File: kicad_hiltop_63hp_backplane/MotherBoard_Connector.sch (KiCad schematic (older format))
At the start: 7 parts, among them J10 Conn_01x02, J7 HILTOP_PCIE-64_CONN, J8 Conn_02x04_Odd_Even, J9 Conn_02x02_Counter_Clockwise

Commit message: Rev A
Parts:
- J10: symbol Connector1:Conn_01x02 -> hiltop_backplane_brd-rescue:Conn_01x02-Connector1; Devtank (none) -> 709-002
- J7: footprint GTI_Footprint_Lib:CONN PCI EXP FEMALE 64POS 0.039 -> Devtank_PCB_Lib:CONN PCI EXP FEMALE 64POS 0.039; symbol gti_Lattice:HILTOP_PCIE-64_CONN -> hiltop_backplane_brd-rescue:HILTOP_PCIE-64_CONN-gti_Lattice
- J8: symbol Connector1:Conn_02x04_Odd_Even -> hiltop_backplane_brd-rescue:Conn_02x04_Odd_Even-Connector1; Devtank (none) -> 709-005
- J9: symbol Connector1:Conn_02x02_Counter_Clockwise -> hiltop_backplane_brd-rescue:Conn_02x02_Counter_Clockwise-Connector1; Devtank (none) -> 709-006
- R45: symbol device:Polyfuse -> hiltop_backplane_brd-rescue:Polyfuse-device; Devtank (none) -> 101-005
- R46, R47: symbol device:Polyfuse -> hiltop_backplane_brd-rescue:Polyfuse-device; Devtank (none) -> 101-007
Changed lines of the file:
@@
 -5V
 $Comp
-L gti_Lattice:HILTOP_PCIE-64_CONN J7
+L hiltop_backplane_brd-rescue:HILTOP_PCIE-64_CONN-gti_Lattice J7
 U 1 1 5C13457D
 P 3575 2725
 F 0 "J7" H 3575 4640 50  0000 C CNN
 F 1 "HILTOP_PCIE-64_CONN" H 3575 4549 50  0000 C CNN
-F 2 "GTI_Footprint_Lib:CONN PCI EXP FEMALE 64POS 0.039" H 2925 4575 50  0001 C CNN
+F 2 "Devtank_PCB_Lib:CONN PCI EXP FEMALE 64POS 0.039" H 2925 4575 50  0001 C CNN
 F 3 "" H 3075 4675 50  0001 C CNN
 	1    3575 2725
@@
 Connection ~ 4650 2175
 $Comp
-L Connector1:Conn_02x04_Odd_Even J8
+L hiltop_backplane_brd-rescue:Conn_02x04_Odd_Even-Connector1 J8
 U 1 1 5C155D60
 P 8400 1825
@@
 F 2 "Connector_Molex:Molex_Mini-Fit_Jr_5566-08A_2x04_P4.20mm_Vertical" H 8400 1825 50  0001 C CNN
 F 3 "~" H 8400 1825 50  0001 C CNN
+F 4 "709-005" H 0   0   50  0001 C CNN "Devtank"
 	1    8400 1825
 	1    0    0    -1
 $EndComp
 $Comp
-L Connector1:Conn_02x02_Counter_Clockwise J9
+L hiltop_backplane_brd-rescue:Conn_02x02_Counter_Clockwise-Connector1 J9
 U 1 1 5C155E73
 P 8425 2700
@@
 F 2 "Connector_Molex:Molex_Mini-Fit_Jr_5566-04A_2x02_P4.20mm_Vertical" H 8425 2700 50  0001 C CNN
 F 3 "~" H 8425 2700 50  0001 C CNN
+F 4 "709-006" H 0   0   50  0001 C CNN "Devtank"
 	1    8425 2700
 	1    0    0    -1
 $EndComp
 $Comp
-L Connector1:Conn_01x02 J10
+L hiltop_backplane_brd-rescue:Conn_01x02-Connector1 J10
 U 1 1 5C155F47
 P 8475 3425
@@
 F 2 "Connector_Molex:Molex_Mini-Fit_Jr_5566-02A2_2x01_P4.20mm_Vertical" H 8475 3425 50  0001 C CNN
 F 3 "~" H 8475 3425 50  0001 C CNN
+F 4 "709-002" H 0   0   50  0001 C CNN "Devtank"
 	1    8475 3425
 	1    0    0    -1
@@
 	8700 2025 8925 2025
 $Comp
-L device:Polyfuse R47
+L hiltop_backplane_brd-rescue:Polyfuse-device R47
 U 1 1 5C36D98A
 P 9100 2700
@@
 F 2 "Resistor_SMD:R_1206_3216Metric" H 9150 2500 50  0001 L CNN
 F 3 "" H 9100 2700 50  0001 C CNN
+F 4 "101-007" H 0   0   50  0001 C CNN "Devtank"
 	1    9100 2700
 	0    1    1    0
 $EndComp
 $Comp
-L device:Polyfuse R45
+L hiltop_backplane_brd-rescue:Polyfuse-device R45
 U 1 1 5C36DB02
 P 7950 2700
@@
 F 2 "Resistor_SMD:R_0603_1608Metric" H 8000 2500 50  0001 L CNN
 F 3 "" H 7950 2700 50  0001 C CNN
+F 4 "101-005" H 0   0   50  0001 C CNN "Devtank"
 	1    7950 2700
 	0    1    1    0
 $EndComp
 $Comp
-L device:Polyfuse R46
+L hiltop_backplane_brd-rescue:Polyfuse-device R46
 U 1 1 5C36DBE2
 P 7950 2800
@@
 F 2 "Resistor_SMD:R_1206_3216Metric" H 8000 2600 50  0001 L CNN
 F 3 "" H 7950 2800 50  0001 C CNN
+F 4 "101-007" H 0   0   50  0001 C CNN "Devtank"
 	1    7950 2800
 	0    1    1    0

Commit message: add latest changes
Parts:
- J10: symbol hiltop_backplane_brd-rescue:Conn_01x02-Connector1 -> hiltop_backplane_brd-rescue:Conn_01x02-Connector1-hiltop_backplane_brd-rescue
- J7: symbol hiltop_backplane_brd-rescue:HILTOP_PCIE-64_CONN-gti_Lattice -> hiltop_backplane_brd-rescue:HILTOP_PCIE-64_CONN-gti_Lattice-hiltop_backplane_brd-rescue
- J8: symbol hiltop_backplane_brd-rescue:Conn_02x04_Odd_Even-Connector1 -> Connector:Conn_02x04_Top_Bottom
- J9: symbol hiltop_backplane_brd-rescue:Conn_02x02_Counter_Clockwise-Connector1 -> Connector:Conn_02x02_Top_Bottom
- R45, R46, R47: symbol hiltop_backplane_brd-rescue:Polyfuse-device -> hiltop_backplane_brd-rescue:Polyfuse-device-hiltop_backplane_brd-rescue
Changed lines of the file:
@@
 EESchema Schematic File Version 4
 LIBS:hiltop_backplane_brd-cache
-EELAYER 26 0
+EELAYER 29 0
 EELAYER END
 $Descr A4 11693 8268
 encoding utf-8
 Sheet 4 6
-Title ""
-Date ""
-Rev ""
-Comp ""
+Title "63HP HILTOP Backplane"
+Date "2020-02-29"
+Rev "B"
+Comp "Devtank Ltd"
 Comment1 ""
 Comment2 ""
@@
 -5V
 $Comp
-L hiltop_backplane_brd-rescue:HILTOP_PCIE-64_CONN-gti_Lattice J7
+L hiltop_backplane_brd-rescue:HILTOP_PCIE-64_CONN-gti_Lattice-hiltop_backplane_brd-rescue J7
 U 1 1 5C13457D
 P 3575 2725
@@
 Connection ~ 4650 2175
 $Comp
-L hiltop_backplane_brd-rescue:Conn_02x04_Odd_Even-Connector1 J8
+L Connector:Conn_02x04_Top_Bottom J8
 U 1 1 5C155D60
 P 8400 1825
@@
 $EndComp
 $Comp
-L hiltop_backplane_brd-rescue:Conn_02x02_Counter_Clockwise-Connector1 J9
+L Connector:Conn_02x02_Top_Bottom J9
 U 1 1 5C155E73
 P 8425 2700
@@
 $EndComp
 $Comp
-L hiltop_backplane_brd-rescue:Conn_01x02-Connector1 J10
+L hiltop_backplane_brd-rescue:Conn_01x02-Connector1-hiltop_backplane_brd-rescue J10
 U 1 1 5C155F47
 P 8475 3425
@@
 	8700 2025 8925 2025
 $Comp
-L hiltop_backplane_brd-rescue:Polyfuse-device R47
+L hiltop_backplane_brd-rescue:Polyfuse-device-hiltop_backplane_brd-rescue R47
 U 1 1 5C36D98A
 P 9100 2700
@@
 $EndComp
 $Comp
-L hiltop_backplane_brd-rescue:Polyfuse-device R45
+L hiltop_backplane_brd-rescue:Polyfuse-device-hiltop_backplane_brd-rescue R45
 U 1 1 5C36DB02
 P 7950 2700
@@
 $EndComp
 $Comp
-L hiltop_backplane_brd-rescue:Polyfuse-device R46
+L hiltop_backplane_brd-rescue:Polyfuse-device-hiltop_backplane_brd-rescue R46
 U 1 1 5C36DBE2
 P 7950 2800

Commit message: started simplifications to design
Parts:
- J8: symbol Connector:Conn_02x04_Top_Bottom -> hiltop_backplane_brd-rescue:Conn_02x04_Top_Bottom-Connector
- J9: symbol Connector:Conn_02x02_Top_Bottom -> hiltop_backplane_brd-rescue:Conn_02x02_Top_Bottom-Connector
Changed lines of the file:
@@
 EESchema Schematic File Version 4
-LIBS:hiltop_backplane_brd-cache
-EELAYER 29 0
+EELAYER 30 0
 EELAYER END
 $Descr A4 11693 8268
@@
 Connection ~ 4650 2175
 $Comp
-L Connector:Conn_02x04_Top_Bottom J8
+L hiltop_backplane_brd-rescue:Conn_02x04_Top_Bottom-Connector J8
 U 1 1 5C155D60
 P 8400 1825
@@
 $EndComp
 $Comp
-L Connector:Conn_02x02_Top_Bottom J9
+L hiltop_backplane_brd-rescue:Conn_02x02_Top_Bottom-Connector J9
 U 1 1 5C155E73
 P 8425 2700

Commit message: updated FPGA/SOC module pinouts
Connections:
- net MBRD_GPIO12: no longer names the net of J7.B30 (GPIO12)
- net MBRD_GPIO13: no longer names the net of J7.B31 (GPIO13)
- net MBRD_GPIO14: no longer names the net of J7.A29 (GPIO14)
- net MBRD_GPIO15: no longer names the net of J7.A30 (GPIO15)
- net MBRD_GPIO16: no longer names the net of J7.A31 (GPIO16)
- net MBRD_RESERVED_0: no longer names the net of J7.A12 (RESERVED)
- net MBRD_RESERVED_1: no longer names the net of J7.A13 (RESERVED)
- net MBRD_RESERVED_2+: no longer names the net of J7.A14 (RESERVED)
- net MBRD_RESERVED_2-: no longer names the net of J7.A15 (RESERVED)
- no-connect marks 0 -> 9
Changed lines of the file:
@@
 Sheet 4 6
 Title "63HP HILTOP Backplane"
-Date "2020-02-29"
-Rev "B"
+Date "2021-02-04"
+Rev "C"
 Comp "Devtank Ltd"
 Comment1 ""
@@
 Text HLabel 2350 4175 0    60   Input ~ 0
 MBRD_SPI1_CS2
-Text HLabel 2350 4275 0    60   Input ~ 0
-MBRD_GPIO12
-Text HLabel 2350 4375 0    60   Input ~ 0
-MBRD_GPIO13
-Text HLabel 4850 4275 2    60   Input ~ 0
-MBRD_GPIO15
-Text HLabel 4850 4375 2    60   Input ~ 0
-MBRD_GPIO16
 Wire Wire Line
 	4650 1175 4650 1475
@@
 Text HLabel 4850 3375 2    60   Input ~ 0
 MBRD_SPI0_CS1
-Text HLabel 4850 2475 2    60   Input ~ 0
-MBRD_RESERVED_0
-Text HLabel 4850 2575 2    60   Input ~ 0
-MBRD_RESERVED_1
-Text HLabel 4850 2675 2    60   Input ~ 0
-MBRD_RESERVED_2+
-Text HLabel 4850 2775 2    60   Input ~ 0
-MBRD_RESERVED_2-
 Text HLabel 4850 1575 2    60   Input ~ 0
 MBRD_PSEL_0
@@
 Wire Wire Line
 	2625 3075 2350 3075
-Text HLabel 4850 4175 2    59   Input ~ 0
-MBRD_GPIO14
+NoConn ~ 4850 4175
+NoConn ~ 4850 4275
+NoConn ~ 4850 4375
+NoConn ~ 2350 4275
+NoConn ~ 2350 4375
+NoConn ~ 4850 2475
+NoConn ~ 4850 2575
+NoConn ~ 4850 2675
+NoConn ~ 4850 2775
 $EndSCHEMATC

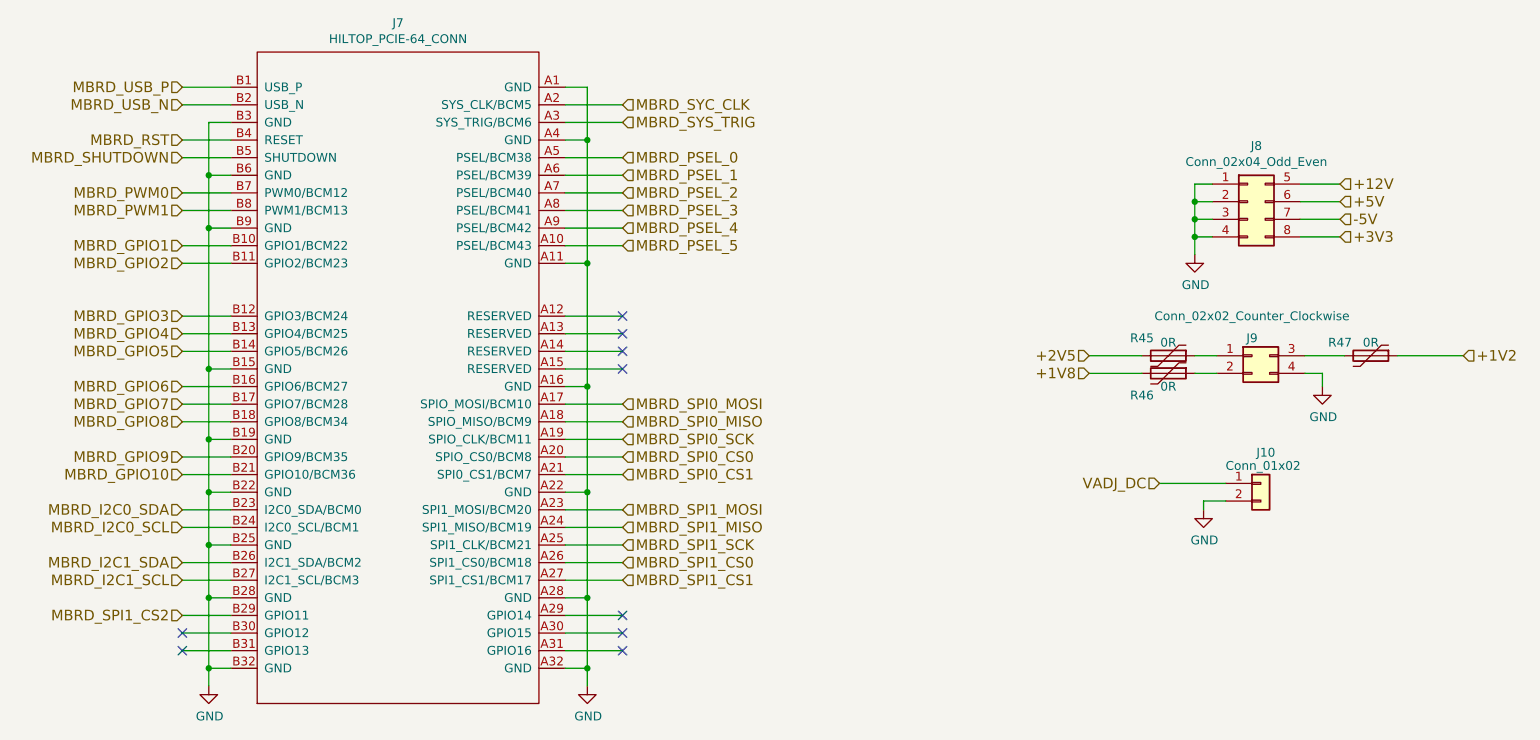
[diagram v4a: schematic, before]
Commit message: updated schematics to RevC including general tidy up
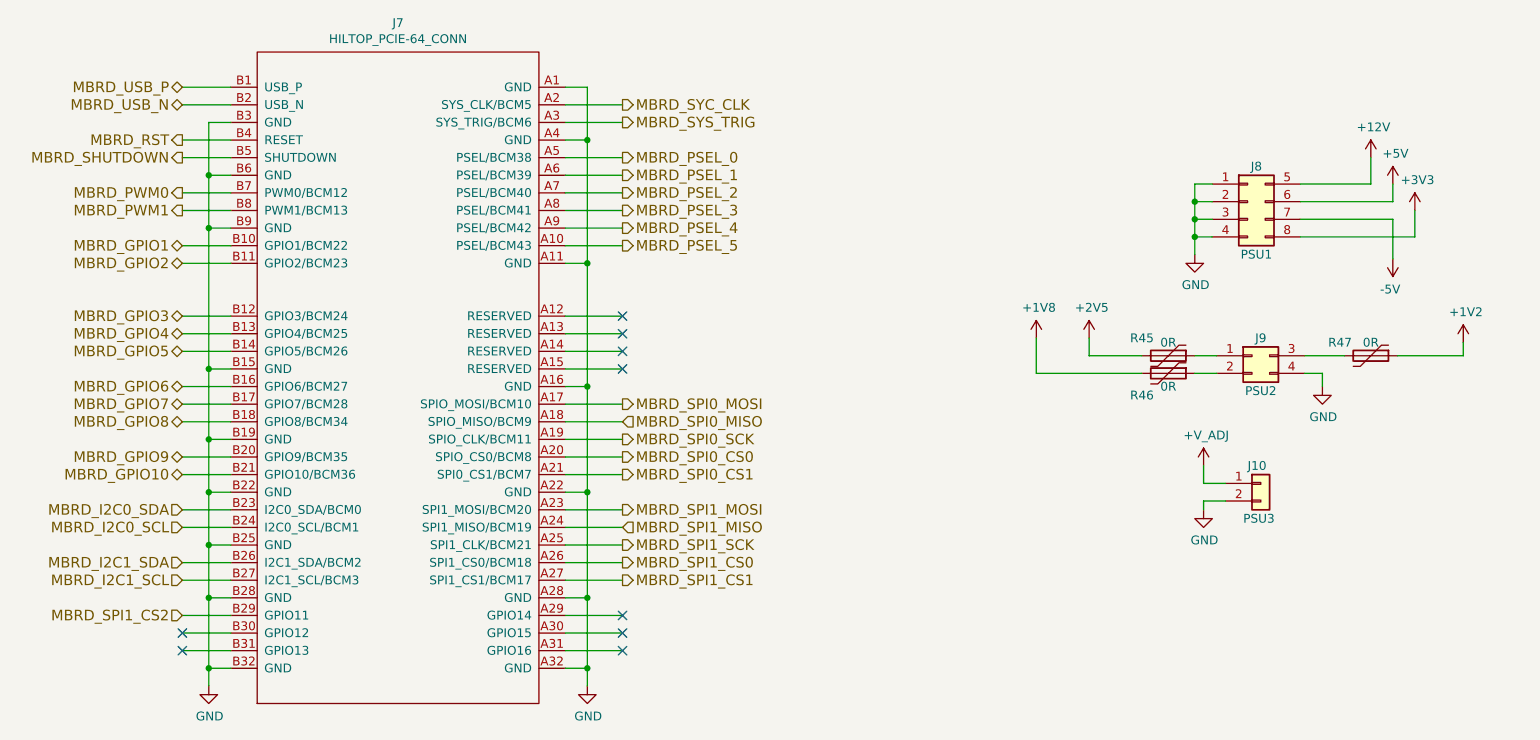
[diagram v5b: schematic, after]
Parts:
- J10: value Conn_01x02 -> PSU3
- J8: value Conn_02x04_Odd_Even -> PSU1
- J9: value Conn_02x02_Counter_Clockwise -> PSU2
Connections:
- net VADJ_DC renamed +V_ADJ
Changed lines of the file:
@@
 $Descr A4 11693 8268
 encoding utf-8
-Sheet 4 6
+Sheet 5 6
 Title "63HP HILTOP Backplane"
 Date "2021-02-04"
@@
 Wire Wire Line
 	4525 4475 4650 4475
-Text HLabel 2350 1175 0    60   Input ~ 0
+Text HLabel 2350 1175 0    60   BiDi ~ 0
 MBRD_USB_P
-Text HLabel 2350 1275 0    60   Input ~ 0
+Text HLabel 2350 1275 0    60   BiDi ~ 0
 MBRD_USB_N
 Wire Wire Line
@@
 Text HLabel 2350 3975 0    60   Input ~ 0
 MBRD_I2C1_SCL
-Text HLabel 2350 1475 0    60   Input ~ 0
+Text HLabel 2350 1475 0    60   Output ~ 0
 MBRD_RST
-Text HLabel 2350 1575 0    60   Input ~ 0
+Text HLabel 2350 1575 0    60   Output ~ 0
 MBRD_SHUTDOWN
-Text HLabel 2350 1775 0    60   Input ~ 0
+Text HLabel 2350 1775 0    60   Output ~ 0
 MBRD_PWM0
-Text HLabel 2350 1875 0    60   Input ~ 0
+Text HLabel 2350 1875 0    60   Output ~ 0
 MBRD_PWM1
-Text HLabel 2350 2075 0    60   Input ~ 0
+Text HLabel 2350 2075 0    60   BiDi ~ 0
 MBRD_GPIO1
-Text HLabel 2350 2175 0    60   Input ~ 0
+Text HLabel 2350 2175 0    60   BiDi ~ 0
 MBRD_GPIO2
-Text HLabel 2350 2475 0    60   Input ~ 0
+Text HLabel 2350 2475 0    60   BiDi ~ 0
 MBRD_GPIO3
-Text HLabel 2350 2575 0    60   Input ~ 0
+Text HLabel 2350 2575 0    60   BiDi ~ 0
 MBRD_GPIO4
-Text HLabel 2350 2675 0    60   Input ~ 0
+Text HLabel 2350 2675 0    60   BiDi ~ 0
 MBRD_GPIO5
-Text HLabel 2350 2875 0    60   Input ~ 0
+Text HLabel 2350 2875 0    60   BiDi ~ 0
 MBRD_GPIO6
-Text HLabel 2350 2975 0    60   Input ~ 0
+Text HLabel 2350 2975 0    60   BiDi ~ 0
 MBRD_GPIO7
-Text HLabel 2350 3075 0    60   Input ~ 0
+Text HLabel 2350 3075 0    60   BiDi ~ 0
 MBRD_GPIO8
-Text HLabel 2350 3275 0    60   Input ~ 0
+Text HLabel 2350 3275 0    60   BiDi ~ 0
 MBRD_GPIO9
-Text HLabel 2350 3375 0    60   Input ~ 0
+Text HLabel 2350 3375 0    60   BiDi ~ 0
 MBRD_GPIO10
-Text HLabel 4850 3575 2    60   Input ~ 0
+Text HLabel 4850 3575 2    60   Output ~ 0
 MBRD_SPI1_MOSI
 Text HLabel 4850 3675 2    60   Input ~ 0
 MBRD_SPI1_MISO
-Text HLabel 4850 3775 2    60   Input ~ 0
+Text HLabel 4850 3775 2    60   Output ~ 0
 MBRD_SPI1_SCK
-Text HLabel 4850 3875 2    60   Input ~ 0
+Text HLabel 4850 3875 2    60   Output ~ 0
 MBRD_SPI1_CS0
-Text HLabel 4850 3975 2    60   Input ~ 0
+Text HLabel 4850 3975 2    60   Output ~ 0
 MBRD_SPI1_CS1
-Text HLabel 4850 2975 2    60   Input ~ 0
+Text HLabel 4850 2975 2    60   Output ~ 0
 MBRD_SPI0_MOSI
 Text HLabel 4850 3075 2    60   Input ~ 0
 MBRD_SPI0_MISO
-Text HLabel 4850 3175 2    60   Input ~ 0
+Text HLabel 4850 3175 2    60   Output ~ 0
 MBRD_SPI0_SCK
-Text HLabel 4850 3275 2    60   Input ~ 0
+Text HLabel 4850 3275 2    60   Output ~ 0
 MBRD_SPI0_CS0
-Text HLabel 4850 3375 2    60   Input ~ 0
+Text HLabel 4850 3375 2    60   Output ~ 0
 MBRD_SPI0_CS1
-Text HLabel 4850 1575 2    60   Input ~ 0
+Text HLabel 4850 1575 2    60   Output ~ 0
 MBRD_PSEL_0
-Text HLabel 4850 1675 2    60   Input ~ 0
+Text HLabel 4850 1675 2    60   Output ~ 0
 MBRD_PSEL_1
-Text HLabel 4850 1775 2    60   Input ~ 0
+Text HLabel 4850 1775 2    60   Output ~ 0
 MBRD_PSEL_2
-Text HLabel 4850 1875 2    60   Input ~ 0
+Text HLabel 4850 1875 2    60   Output ~ 0
 MBRD_PSEL_3
-Text HLabel 4850 1975 2    60   Input ~ 0
+Text HLabel 4850 1975 2    60   Output ~ 0
 MBRD_PSEL_4
-Text HLabel 4850 2075 2    60   Input ~ 0
+Text HLabel 4850 2075 2    60   Output ~ 0
 MBRD_PSEL_5
-Text HLabel 4850 1275 2    60   Input ~ 0
+Text HLabel 4850 1275 2    60   Output ~ 0
 MBRD_SYC_CLK
-Text HLabel 4850 1375 2    60   Input ~ 0
+Text HLabel 4850 1375 2    60   Output ~ 0
 MBRD_SYS_TRIG
-Text HLabel 8925 1725 2    60   Input ~ 0
-+12V
-Text HLabel 8925 1825 2    60   Input ~ 0
-+5V
-Text HLabel 8925 2025 2    60   Input ~ 0
-+3V3
-Text HLabel 8925 1925 2    60   Input ~ 0
--5V
 $Comp
 L hiltop_backplane_brd-rescue:HILTOP_PCIE-64_CONN-gti_Lattice-hiltop_backplane_brd-rescue J7
@@
 U 1 1 5C155D60
 P 8400 1825
-F 0 "J8" H 8450 2142 50  0000 C CNN
-F 1 "Conn_02x04_Odd_Even" H 8450 2051 50  0000 C CNN
+F 0 "J8" H 8450 2025 50  0000 C CNN
+F 1 "PSU1" H 8450 1525 50  0000 C CNN
 F 2 "Connector_Molex:Molex_Mini-Fit_Jr_5566-08A_2x04_P4.20mm_Vertical" H 8400 1825 50  0001 C CNN
 F 3 "~" H 8400 1825 50  0001 C CNN
@@
 U 1 1 5C155E73
 P 8425 2700
-F 0 "J9" H 8425 2800 50  0000 C CNN
-F 1 "Conn_02x02_Counter_Clockwise" H 8425 2925 50  0000 C CNN
+F 0 "J9" H 8475 2800 50  0000 C CNN
+F 1 "PSU2" H 8475 2500 50  0000 C CNN
 F 2 "Connector_Molex:Molex_Mini-Fit_Jr_5566-04A_2x02_P4.20mm_Vertical" H 8425 2700 50  0001 C CNN
 F 3 "~" H 8425 2700 50  0001 C CNN
@@
 U 1 1 5C155F47
 P 8475 3425
-F 0 "J10" H 8450 3600 50  0000 L CNN
-F 1 "Conn_01x02" H 8275 3525 50  0000 L CNN
+F 0 "J10" H 8400 3525 50  0000 L CNN
+F 1 "PSU3" H 8375 3225 50  0000 L CNN
 F 2 "Connector_Molex:Molex_Mini-Fit_Jr_5566-02A2_2x01_P4.20mm_Vertical" H 8475 3425 50  0001 C CNN
 F 3 "~" H 8475 3425 50  0001 C CNN
@@
 Wire Wire Line
 	8825 2800 8825 2875
-Text HLabel 7500 2700 0    60   Input ~ 0
-+2V5
-Text HLabel 7500 2800 0    60   Input ~ 0
-+1V8
-Text HLabel 9625 2700 2    60   Input ~ 0
-+1V2
 $Comp
 L power:GND #PWR034
@@
 	1    0    0    -1
 $EndComp
-Text HLabel 7900 3425 0    60   Input ~ 0
-VADJ_DC
 $Comp
 L power:GND #PWR033
@@
 	8725 2700 8950 2700
 Wire Wire Line
-	7900 3425 8275 3425
-Wire Wire Line
-	8700 1725 8925 1725
-Wire Wire Line
-	8700 1825 8925 1825
-Wire Wire Line
-	8700 1925 8925 1925
-Wire Wire Line
-	8700 2025 8925 2025
+	8150 3425 8275 3425
 $Comp
 L hiltop_backplane_brd-rescue:Polyfuse-device-hiltop_backplane_brd-rescue R47
@@
 	7500 2700 7800 2700
 Wire Wire Line
-	7500 2800 7800 2800
-Wire Wire Line
 	2500 1975 2500 2775
 Wire Wire Line
@@
 NoConn ~ 4850 2675
 NoConn ~ 4850 2775
+$Comp
+L power:+2V5 #PWR?
+U 1 1 60E655E6
+P 7500 2600
+AR Path="/5A077BA2/60E655E6" Ref="#PWR?"  Part="1"
+AR Path="/5C074E5E/60E655E6" Ref="#PWR0130"  Part="1"
+F 0 "#PWR0130" H 7500 2450 50  0001 C CNN
+F 1 "+2V5" H 7515 2773 50  0000 C CNN
+F 2 "" H 7500 2600 50  0001 C CNN
+F 3 "" H 7500 2600 50  0001 C CNN
+	1    7500 2600
+	1    0    0    -1
+$EndComp
+$Comp
+L power:+3V3 #PWR?
+U 1 1 60E655EC
+P 9350 1875
+AR Path="/5A077BA2/60E655EC" Ref="#PWR?"  Part="1"
+AR Path="/5C074E5E/60E655EC" Ref="#PWR0131"  Part="1"
+F 0 "#PWR0131" H 9350 1725 50  0001 C CNN
+F 1 "+3V3" H 9365 2048 50  0000 C CNN
+F 2 "" H 9350 1875 50  0001 C CNN
+F 3 "" H 9350 1875 50  0001 C CNN
+	1    9350 1875
+	1    0    0    -1
+$EndComp
+$Comp
+L power:+1V2 #PWR?
+U 1 1 60E655F2
+P 9625 2625
+AR Path="/5A077BA2/60E655F2" Ref="#PWR?"  Part="1"
+AR Path="/5C074E5E/60E655F2" Ref="#PWR0132"  Part="1"
+F 0 "#PWR0132" H 9625 2475 50  0001 C CNN
+F 1 "+1V2" H 9640 2798 50  0000 C CNN
+F 2 "" H 9625 2625 50  0001 C CNN
+F 3 "" H 9625 2625 50  0001 C CNN
+	1    9625 2625
+	1    0    0    -1
+$EndComp
+$Comp
+L power:+1V8 #PWR?
+U 1 1 60E655F8
+P 7200 2600
+AR Path="/5A077BA2/60E655F8" Ref="#PWR?"  Part="1"
+AR Path="/5C074E5E/60E655F8" Ref="#PWR0133"  Part="1"
+F 0 "#PWR0133" H 7200 2450 50  0001 C CNN
+F 1 "+1V8" H 7215 2773 50  0000 C CNN
+F 2 "" H 7200 2600 50  0001 C CNN
+F 3 "" H 7200 2600 50  0001 C CNN
+	1    7200 2600
+	1    0    0    -1
+$EndComp
+Wire Wire Line
+	9625 2625 9625 2700
+Wire Wire Line
+	7500 2600 7500 2700
+Wire Wire Line
+	7200 2600 7200 2800
+Wire Wire Line
+	7200 2800 7800 2800
+$Comp
+L power:+5V #PWR0134
+U 1 1 62F4211C
+P 9225 1725
+F 0 "#PWR0134" H 9225 1575 50  0001 C CNN
+F 1 "+5V" H 9240 1898 50  0000 C CNN
+F 2 "" H 9225 1725 50  0001 C CNN
+F 3 "" H 9225 1725 50  0001 C CNN
+	1    9225 1725
+	1    0    0    -1
+$EndComp
+$Comp
+L Devtank:-5V #PWR0135
+U 1 1 62F42915
+P 9225 2150
+F 0 "#PWR0135" H 9225 2000 50  0001 C CNN
+F 1 "-5V" H 9240 2323 50  0000 C CNN
+F 2 "" H 9225 2150 50  0000 C CNN
+F 3 "" H 9225 2150 50  0000 C CNN
+	1    9225 2150
+	-1   0    0    1
+$EndComp
+$Comp
+L power:+12V #PWR0136
+U 1 1 62F432BB
+P 9100 1575
+F 0 "#PWR0136" H 9100 1425 50  0001 C CNN
+F 1 "+12V" H 9115 1748 50  0000 C CNN
+F 2 "" H 9100 1575 50  0001 C CNN
+F 3 "" H 9100 1575 50  0001 C CNN
+	1    9100 1575
+	1    0    0    -1
+$EndComp
+Wire Wire Line
+	9100 1725 9100 1575
+Wire Wire Line
+	8700 1725 9100 1725
+Wire Wire Line
+	9225 1825 9225 1725
+Wire Wire Line
+	8700 1825 9225 1825
+Wire Wire Line
+	9350 1875 9350 2025
+Wire Wire Line
+	8700 2025 9350 2025
+Wire Wire Line
+	9225 1925 9225 2150
+Wire Wire Line
+	8700 1925 9225 1925
+$Comp
+L Devtank:+V_ADJ #PWR0137
+U 1 1 62F6F17A
+P 8150 3325
+F 0 "#PWR0137" H 8150 3175 50  0001 C CNN
+F 1 "+V_ADJ" H 8165 3498 50  0000 C CNN
+F 2 "" H 8150 3325 50  0000 C CNN
+F 3 "" H 8150 3325 50  0000 C CNN
+	1    8150 3325
+	1    0    0    -1
+$EndComp
+Wire Wire Line
+	8150 3425 8150 3325
 $EndSCHEMATC

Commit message: noticed a fpga_Soc module missing on schematics
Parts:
- R45: footprint Resistor_SMD:R_0603_1608Metric -> Resistor_SMD:R_1206_3216Metric
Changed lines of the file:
@@
 F 0 "R45" V 7850 2550 50  0000 C CNN
 F 1 "0R" V 7875 2700 50  0000 C CNN
-F 2 "Resistor_SMD:R_0603_1608Metric" H 8000 2500 50  0001 L CNN
+F 2 "Resistor_SMD:R_1206_3216Metric" H 8000 2500 50  0001 L CNN
 F 3 "" H 7950 2700 50  0001 C CNN
 F 4 "101-005" H 0   0   50  0001 C CNN "Devtank"
